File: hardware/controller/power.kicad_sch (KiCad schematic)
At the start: 0 parts

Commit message: add IMU, FLOW, 5V, 3.3V, MOSFET SW
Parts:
- added C19: 100n/16V, Capacitor_SMD:C_0603_1608Metric, symbol Device:C
- added C20, C23: 100n, Capacitor_SMD:C_0603_1608Metric, symbol Device:C
- added C21, C22: 4.7u, Capacitor_SMD:C_0603_1608Metric, symbol Device:C
- added C24: 10u/50V, Capacitor_SMD:C_1206_3216Metric, symbol Device:C
- added C25, C26: 47u/16V, Capacitor_SMD:C_1206_3216Metric, symbol Device:C
- added C27: 22n, Capacitor_SMD:C_0603_1608Metric, symbol Device:C
- added D5: SK56, Diode_SMD:D_SMB, symbol Device:D_Schottky
- added D6: RED, LED_SMD:LED_0603_1608Metric, symbol Device:LED
- added J3: XT-60, goose:XT60PW-M, symbol Connector_Generic:Conn_01x02
- added L1: 6.8u/4.5A, goose:PA4341.XXXNLT, symbol Device:L
- added Q1: IRFR5305, symbol Device:Q_PMOS_GDS
- added R12: 10k, Resistor_SMD:R_0603_1608Metric, symbol Device:R
- added R13, R17: 1k, Resistor_SMD:R_0603_1608Metric, symbol Device:R
- added R14: 100k, Resistor_SMD:R_0603_1608Metric, symbol Device:R
- added R15: 49.9k, Resistor_SMD:R_0603_1608Metric, symbol Device:R
- added R16: 17.8k, Resistor_SMD:R_0603_1608Metric, symbol Device:R
- added SW4: JS102011SAQN, symbol Switch:SW_Push_SPDT
- added U5: LM1117MP-3.3, Package_TO_SOT_SMD:SOT-223-3_TabPin2, symbol Regulator_Linear:LM1117MP-3.3
- added U6: LV14340, symbol hogger2:LV14340
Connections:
- new net: C19.1, U6.1 (BOOT)
- new net: R15.1, U6.4 (RT/SYNC)
- new net: R14.2, R16.1, U6.5 (FB)
- new net: C27.1, U6.6 (SS)
- new net: C19.2, D5.1 (K), L1.1, U6.8 (SW)
- new net: Q1.1 (G), R12.2, R13.1
- new net: R13.2, SW4.2 (B)
- new net: D6.2 (A), R17.2
- new net +3.3V: C22.1, C23.1, R17.1, U5.2 (VO)
- new net +5V: C20.1, C21.1, C25.1, C26.1, L1.2, R14.1, U5.3 (VI)
- new net BATTERY_IN: J3.2 (Pin_2), Q1.3 (S), R12.1
- new net GND: C20.2, C21.2, C22.2, C23.2, C24.2, C25.2, C26.2, C27.2, D5.2 (A), D6.1 (K), J3.1 (Pin_1), R15.2, R16.2, SW4.1 (A), U5.1 (GND), U6.7 (GND), U6.9 (PAD)
- new net VBUS: C24.1, Q1.2 (D), U6.2 (VIN)
- no-connect marks 0 -> 2
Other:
- note added: "3.3V domain"
- note added: "5V domain"
- note added: "czy serwa będą działać lepiej na wyższym napięciu? 6V lub 7V"
- note added: "potrzebna większa przetwornica? ta ma 3.5A/40V"
- note added: "potrzebny większy MOSFET? ten ma 31A/55V"
- note added: "power input"
- note added: "should be 0.75V"

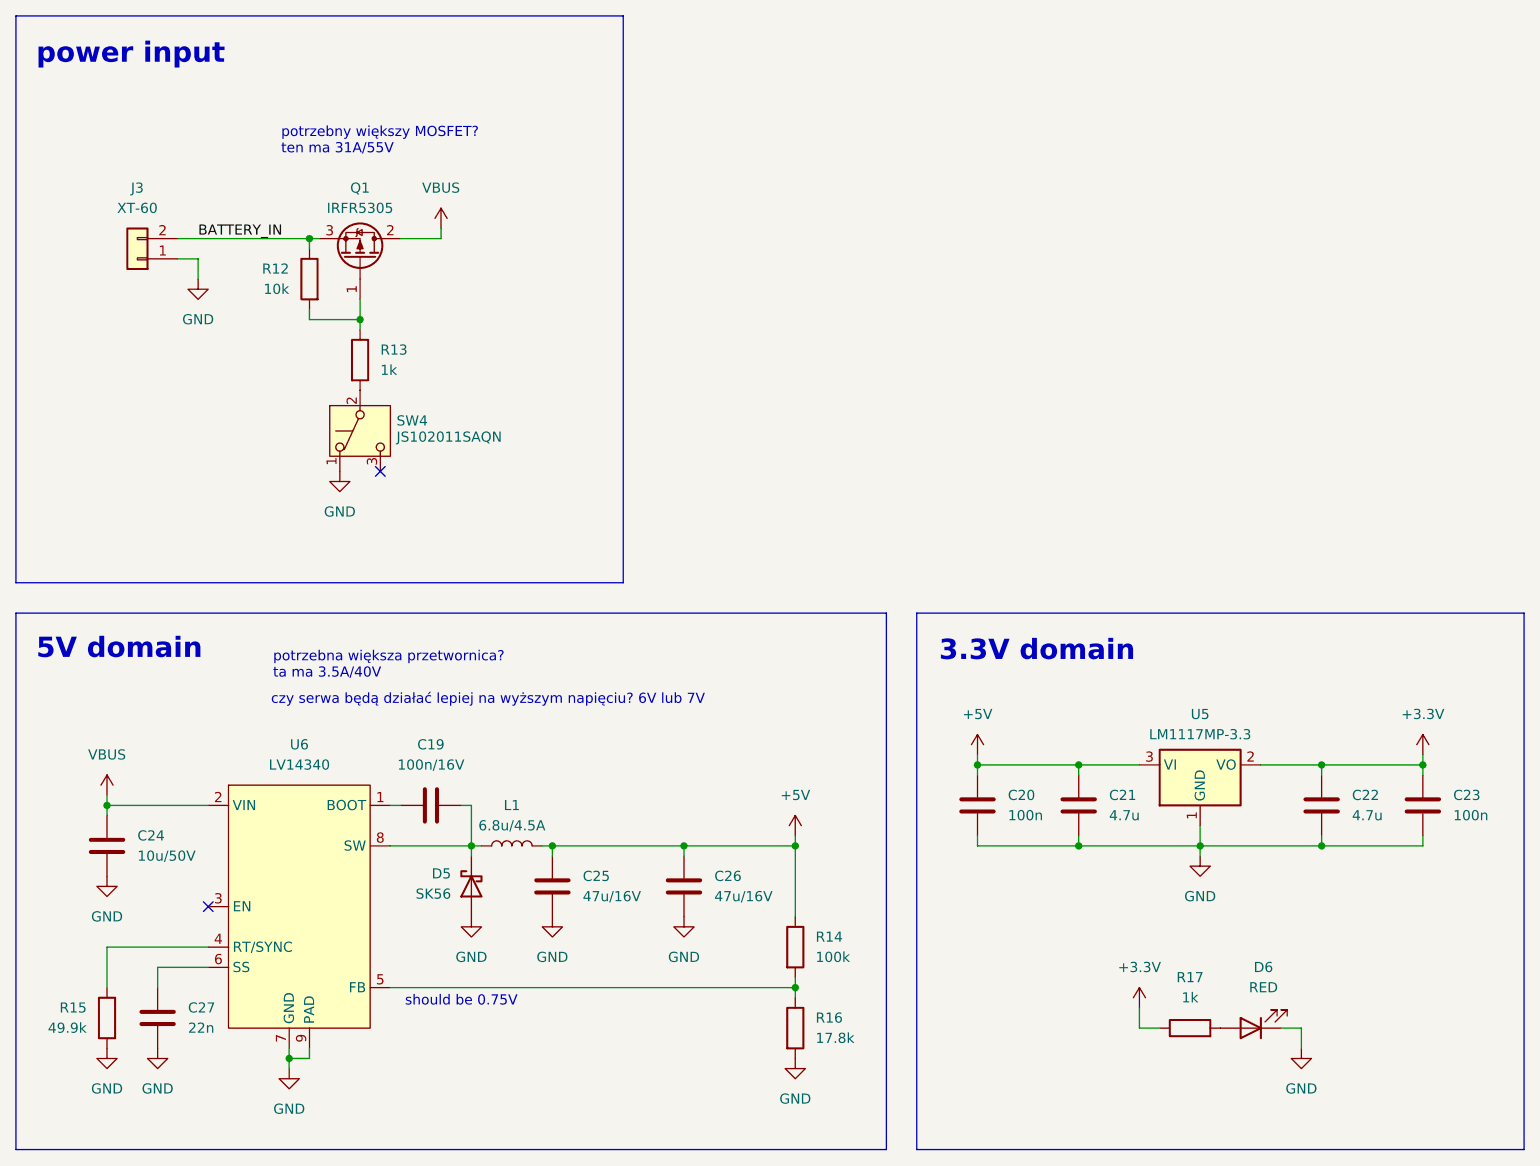
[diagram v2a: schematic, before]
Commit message: change P-MOSFET on the battery enter
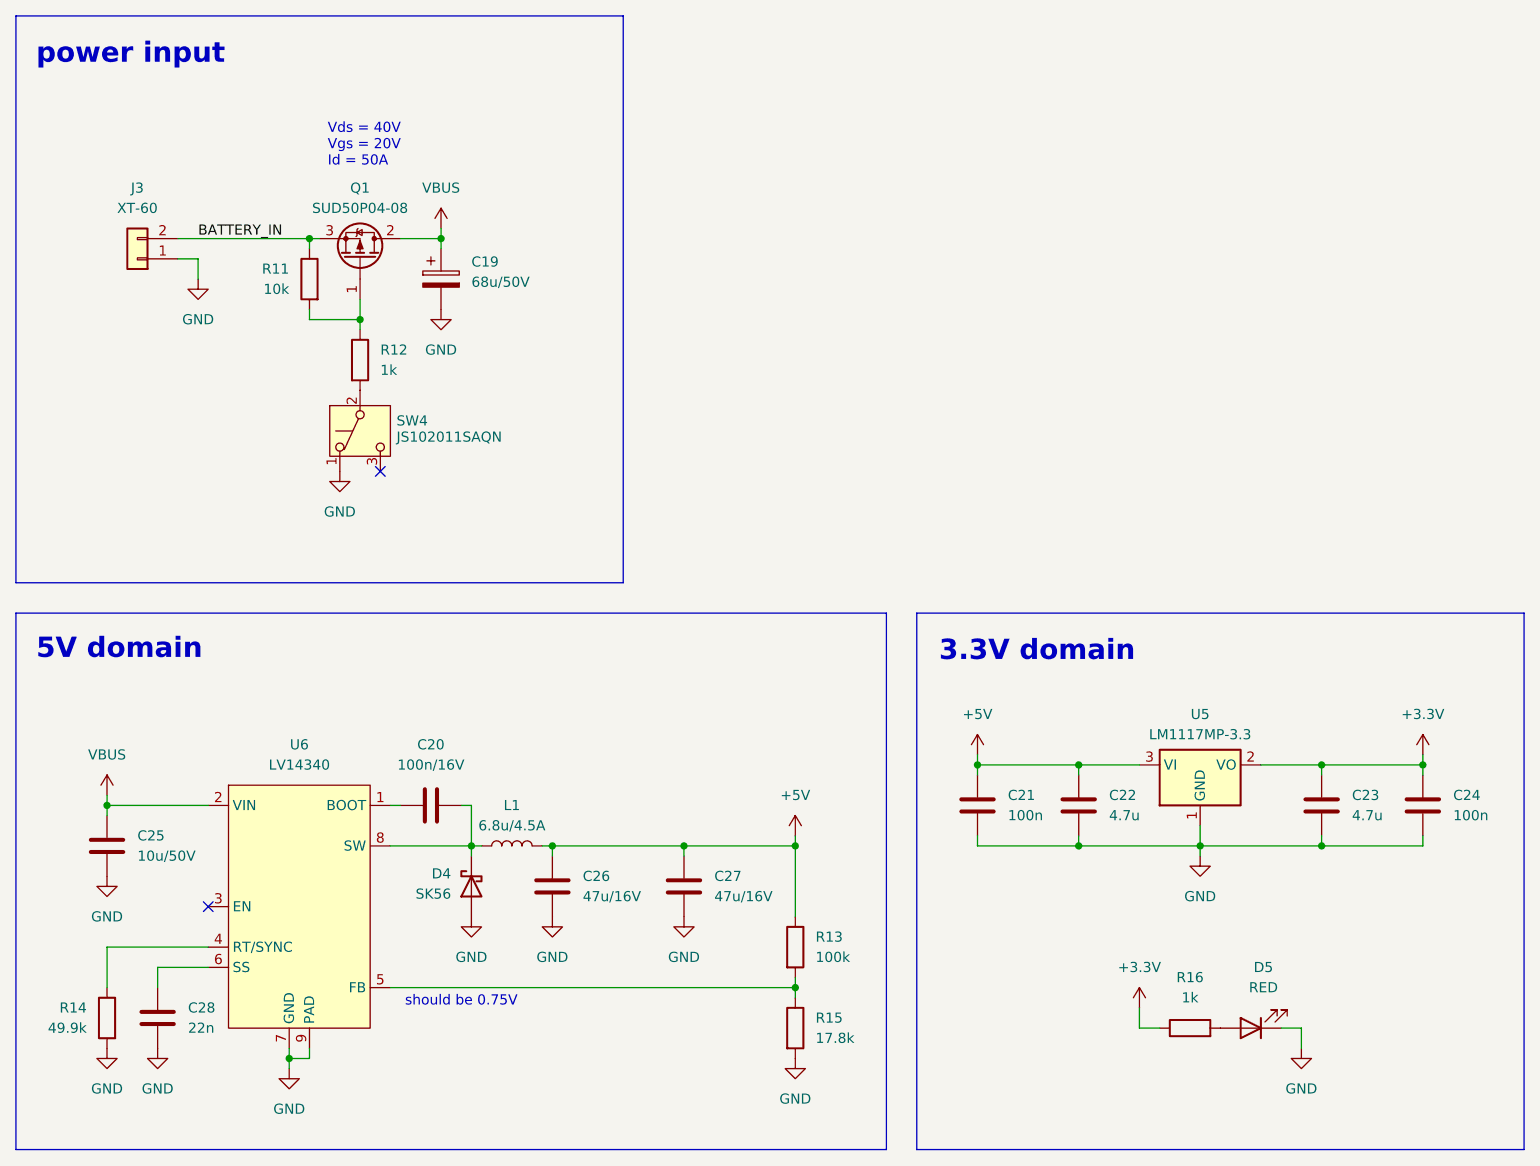
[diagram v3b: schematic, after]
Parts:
- removed Q1: IRFR5305, symbol Device:Q_PMOS_GDS
- added C19: 68u/50V, symbol Device:C_Polarized
- added Q1: SUD50P04-08, Package_TO_SOT_SMD:TO-252-2, symbol Transistor_FET:SUD50P04-08
- renumbered C19 to C20, C20 to C21, C21 to C22, C22 to C23, C23 to C24, C24 to C25, C25 to C26, C26 to C27, C27 to C28, D5 to D4, D6 to D5, R12 to R11, R13 to R12, R14 to R13, R15 to R14, R16 to R15, R17 to R16
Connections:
- net BATTERY_IN: now also Q1.3 (S)
- net GND: now also C19.2
- net VBUS: now also C19.1, Q1.2 (D)
- net at R11.2, R12.1: now also Q1.1 (G)
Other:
- note added: "Vds = 40V Vgs = 20V Id = 50A"
- note removed: "czy serwa będą działać lepiej na wyższym napięciu? 6V lub 7V"
- note removed: "potrzebna większa przetwornica? ta ma 3.5A/40V"
- note removed: "potrzebny większy MOSFET? ten ma 31A/55V"

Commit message: footprints, layout
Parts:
- added C19: 47u/50V, Capacitor_SMD:CP_Elec_6.3x7.7, symbol Device:C_Polarized
- C20: renamed from C19; value 68u/50V -> 47u/50V; footprint (none) -> Capacitor_SMD:CP_Elec_6.3x7.7
- J3: footprint goose:XT60PW-M -> Connector_AMASS:AMASS_XT60PW-M_1x02_P7.20mm_Horizontal
- L1: footprint goose:PA4341.XXXNLT -> (none)
- SW4: footprint (none) -> Button_Switch_SMD:SW_SPDT_CK_JS102011SAQN
- U6: footprint (none) -> Package_SO:SOIC-8-1EP_3.9x4.9mm_P1.27mm_EP2.514x3.2mm_ThermalVias
- renumbered C20 to C21, C21 to C22, C22 to C23, C23 to C24, C24 to C25, C25 to C26, C26 to C27, C27 to C28, C28 to C29
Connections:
- net BATTERY_IN: now also C19.1
- net GND: now also C19.2
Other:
- moved on the sheet: C20, Q1, R11, R12, SW4

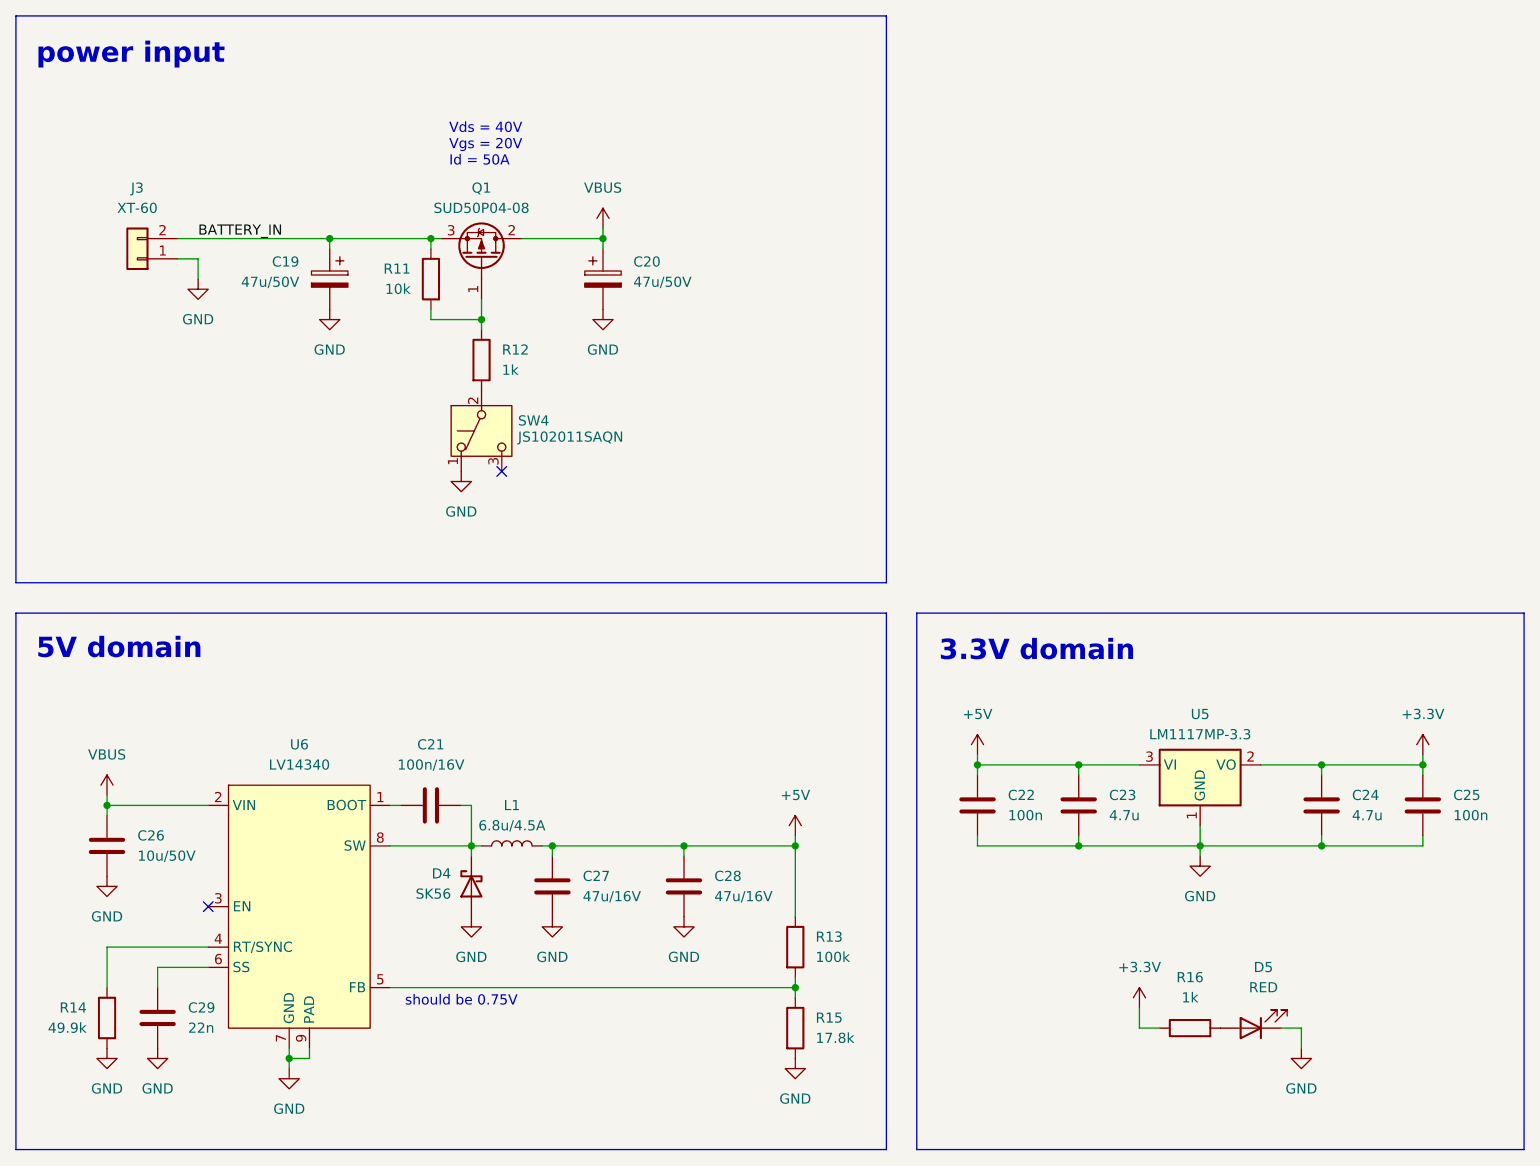
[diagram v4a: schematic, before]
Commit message: add VBUS sense to STM and ESP, change buttons and sw to vertical, add USB-C to SEM
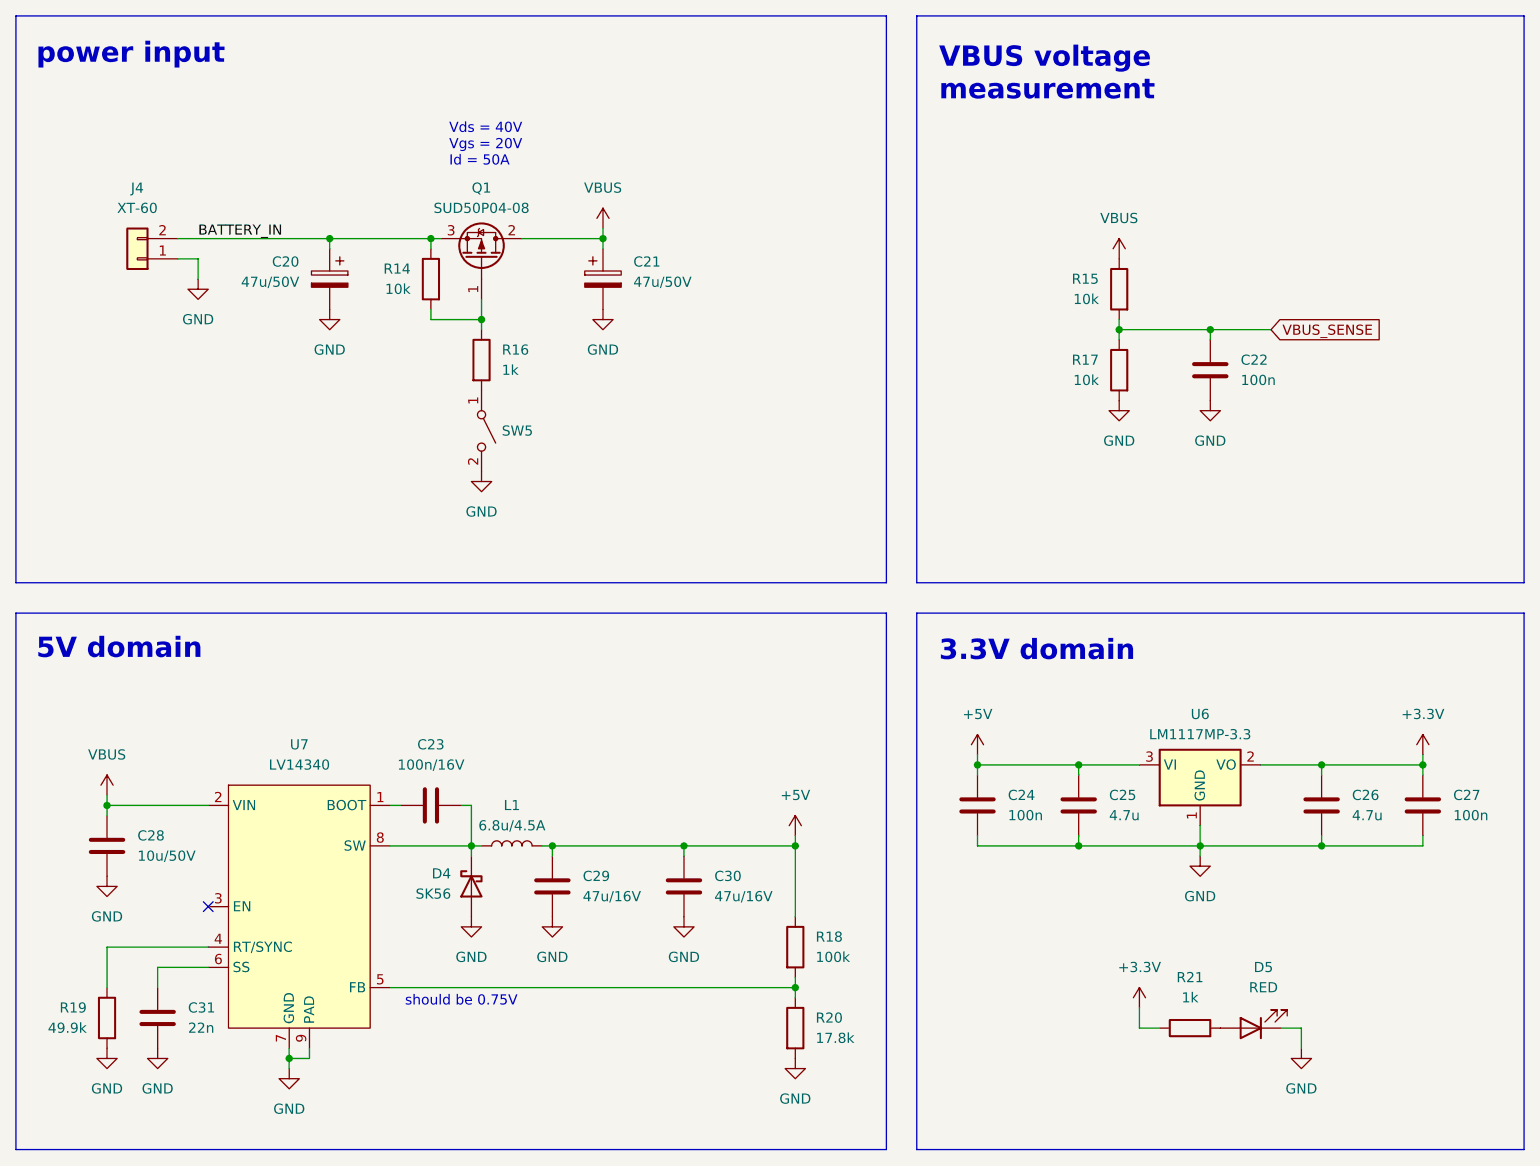
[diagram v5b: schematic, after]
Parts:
- removed SW4: JS102011SAQN, Button_Switch_SMD:SW_SPDT_CK_JS102011SAQN, symbol Switch:SW_Push_SPDT
- added C22: 100n, Capacitor_SMD:C_0603_1608Metric, symbol Device:C
- added R15, R17: 10k, Resistor_SMD:R_0603_1608Metric, symbol Device:R
- added SW5: SW_SPST, Button_Switch_THT:SW_CK_JS202011CQN_DPDT_Straight, symbol Switch:SW_SPST
- renumbered C19 to C20, C20 to C21, C21 to C23, C22 to C24, C23 to C25, C24 to C26, C25 to C27, C26 to C28, C27 to C29, C28 to C30, C29 to C31, J3 to J4, R11 to R14, R12 to R16, R13 to R18, R14 to R19, R15 to R20, R16 to R21, U5 to U6, U6 to U7
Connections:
- net GND: now also C22.2, R17.2, SW5.2 (B)
- net VBUS: now also R15.1
- net at R16.2: now also SW5.1 (A)
- new net VBUS_SENSE: C22.1, R15.2, R17.1
- no-connect marks 2 -> 1
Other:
- note added: "VBUS voltage measurement"

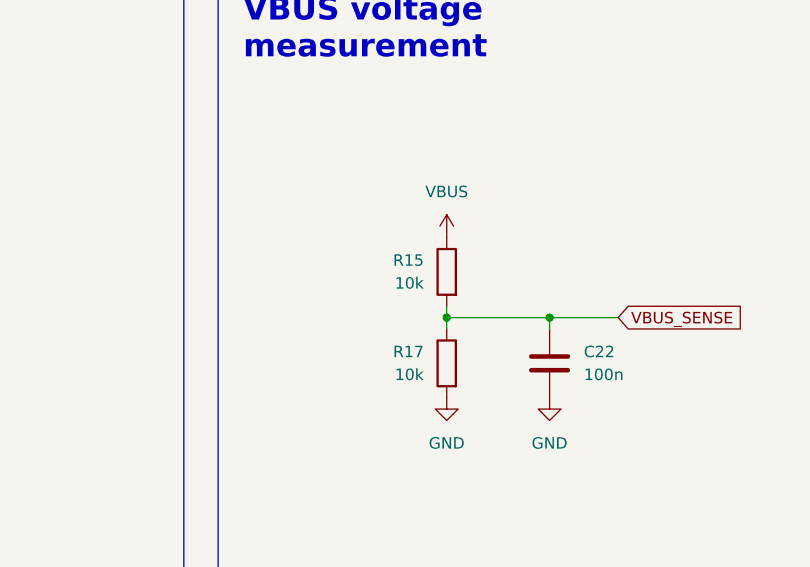
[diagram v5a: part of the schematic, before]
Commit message: fix voltage divider
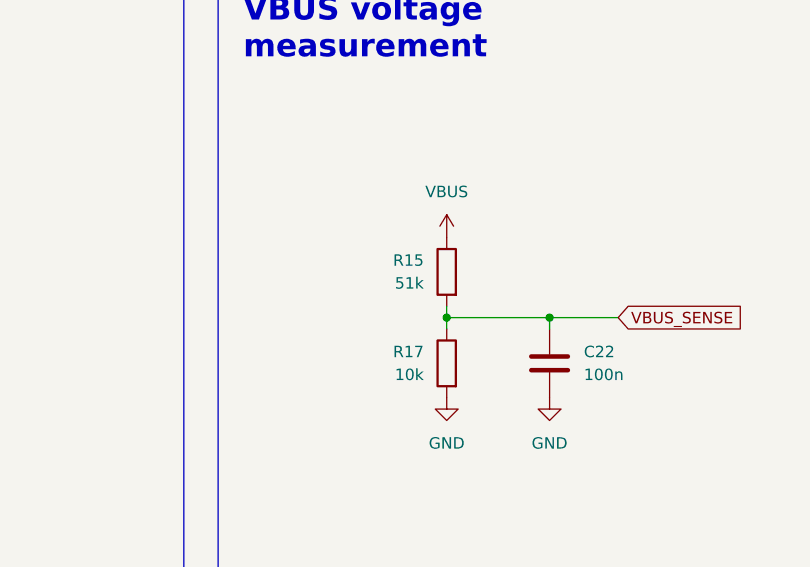
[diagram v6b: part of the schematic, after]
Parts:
- R15: value 10k -> 51k
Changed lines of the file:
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@@
 			)
 		)
-		(property "Value" "10k"
+		(property "Value" "51k"
 			(at 154.94 54.6099 0)
 			(effects

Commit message: custom footprints with all 3D models
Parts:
- removed C20, C21: 47u/50V, Capacitor_SMD:CP_Elec_6.3x7.7, symbol Device:C_Polarized
- J4: footprint Connector_AMASS:AMASS_XT60PW-M_1x02_P7.20mm_Horizontal -> hogger2:XT60PW-M
- L1: footprint (none) -> hogger2:PA4341.XXXNLT
- U7: footprint Package_SO:SOIC-8-1EP_3.9x4.9mm_P1.27mm_EP2.514x3.2mm_ThermalVias -> hogger2:LV14340
- renumbered C22 to C20, C23 to C21, C24 to C22, C25 to C23, C26 to C24, C27 to C25, C28 to C26, C29 to C27, C30 to C28, C31 to C29
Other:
- moved on the sheet: C20, J4
